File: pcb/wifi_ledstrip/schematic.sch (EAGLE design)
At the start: 44 parts, among them IC1 STM32F10XCXT6, Q1 8MHz

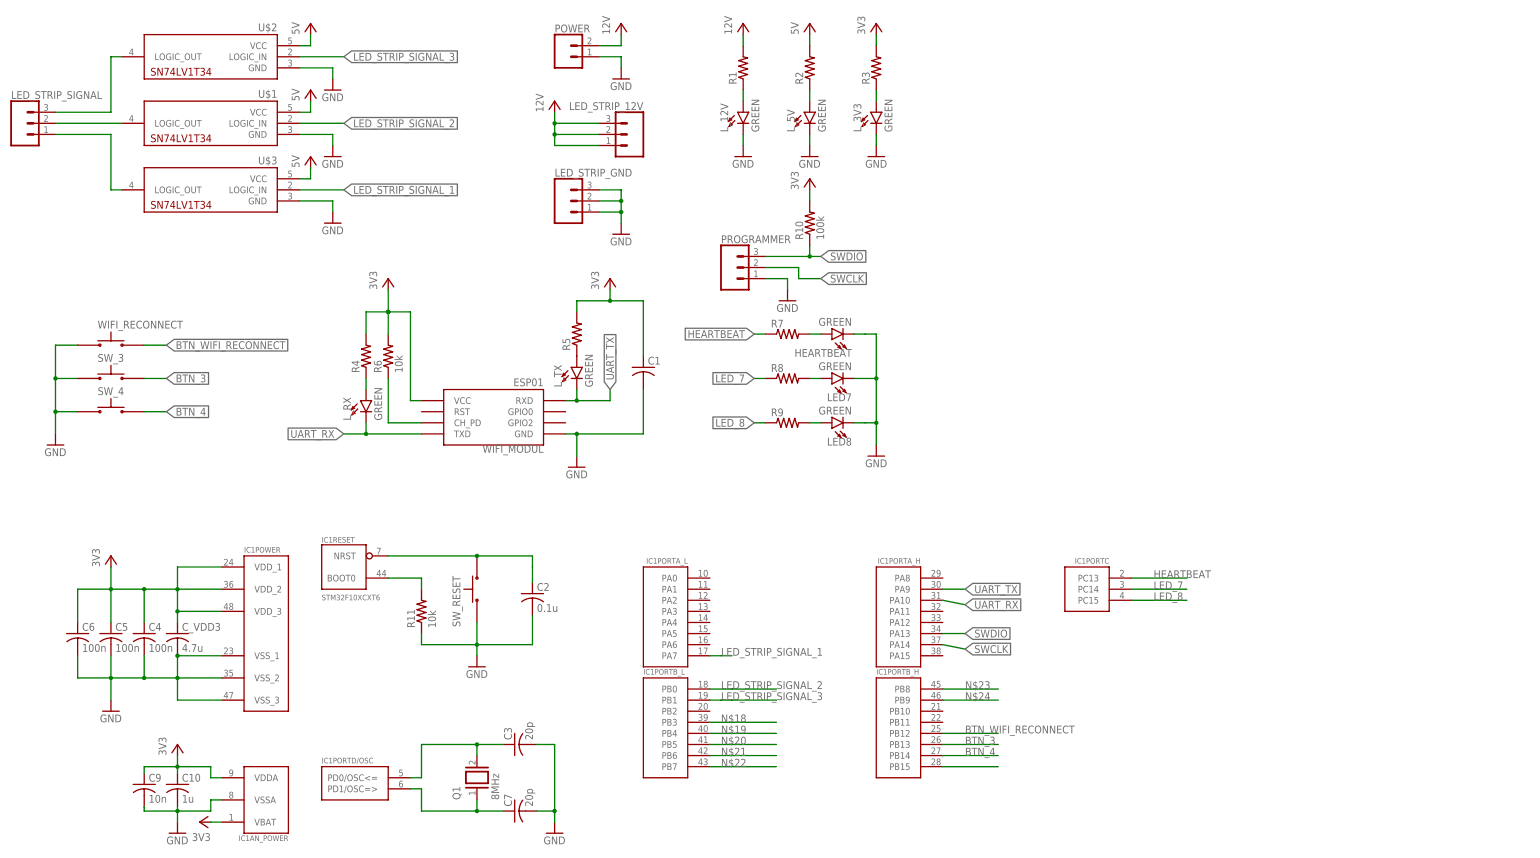
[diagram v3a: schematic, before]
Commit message: parts added, psu symbols fixed
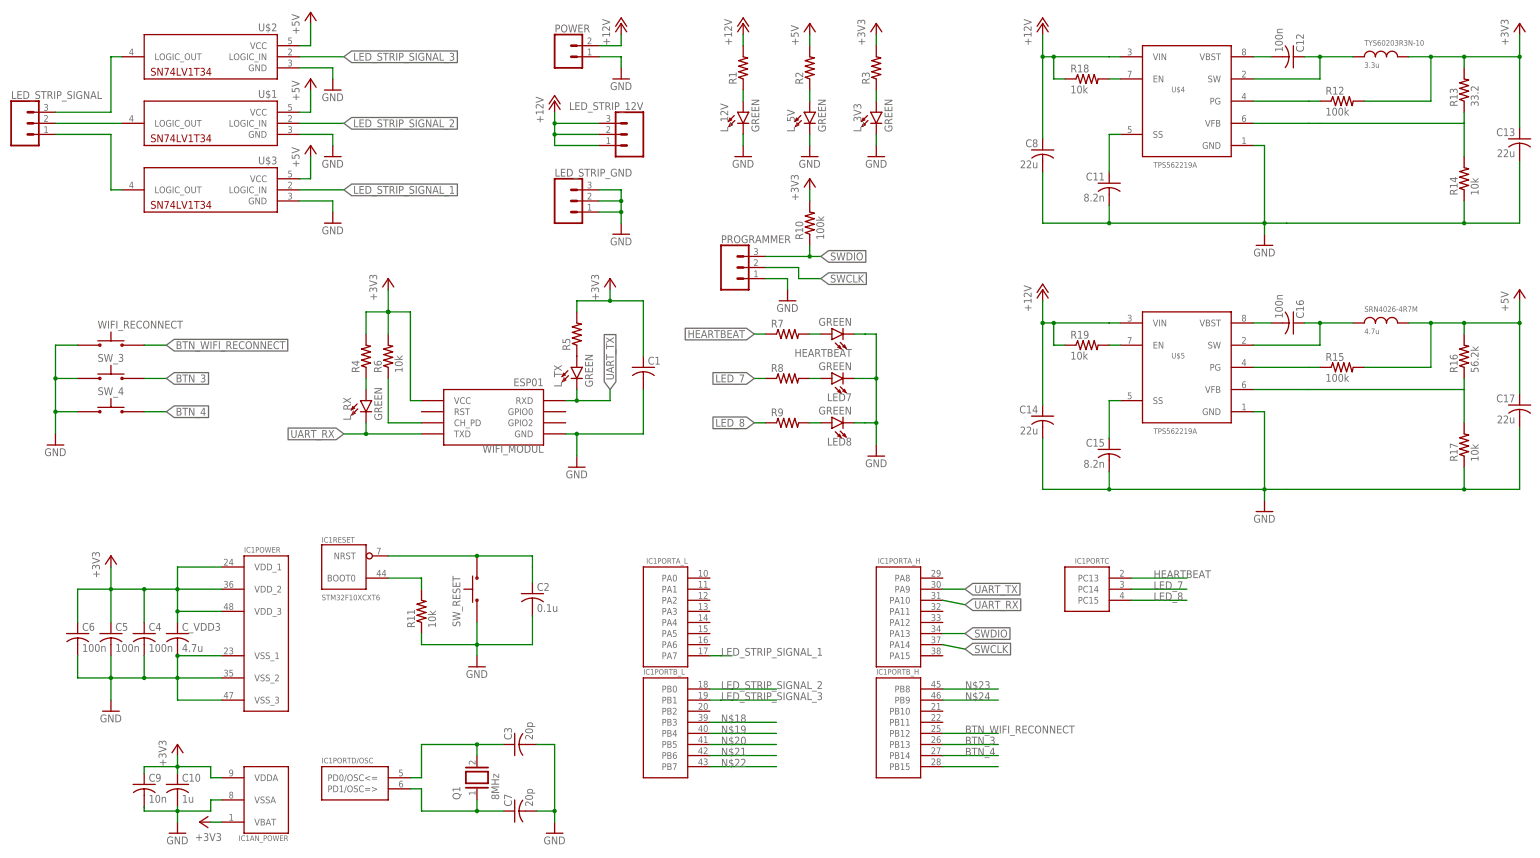
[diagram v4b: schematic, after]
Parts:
- added C11, C15: 8.2n, rcl:C-USC1206
- added C12, C16: 100n, rcl:C-USC1206
- added C13, C14, C17, C8: 22u, rcl:C-USC1206
- added R12, R15: 100k, rcl:R-US_R1206
- added R13: 33.2, rcl:R-US_R1206
- added R14, R17, R18, R19: 10k, rcl:R-US_R1206
- added R16: 56.2k, rcl:R-US_R1206
- added SRN4026-4R7M: 4.7u, mylibrary:SRN4026-4R7M
- added TYS60203R3N-10: 3.3u, mylibrary:TYS60203R3N-10
- added U$4, U$5: TPS562219A, mylibrary:TPS562219A
- U$2: SPICEPREFIX (none) -> U
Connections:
- removed net VCC: C1.1, C10.1, C4.1, C5.1, C6.1, C9.1, C_VDD3.1, IC1AN_POWER.VBAT, IC1AN_POWER.VDDA, IC1POWER.VDD_1, IC1POWER.VDD_2, IC1POWER.VDD_3, LED_STRIP_12V.1, LED_STRIP_12V.2, LED_STRIP_12V.3, POWER.2, R1.2, R10.2, R2.2, R3.2, R4.2, R5.2, R6.2, U$1.VCC, U$2.VCC, U$3.VCC, WIFI_MODUL.VCC
- new net +12V: C14.1, C8.1, LED_STRIP_12V.1, LED_STRIP_12V.2, LED_STRIP_12V.3, POWER.2, R1.2, R18.1, R19.1, U$4.VIN, U$5.VIN
- new net +3V3: C1.1, C10.1, C13.1, C4.1, C5.1, C6.1, C9.1, C_VDD3.1, IC1AN_POWER.VBAT, IC1AN_POWER.VDDA, IC1POWER.VDD_1, IC1POWER.VDD_2, IC1POWER.VDD_3, R10.2, R12.2, R13.2, R3.2, R4.2, R5.2, R6.2, TYS60203R3N-10.2, WIFI_MODUL.VCC
- new net +5V: C17.1, R15.2, R16.2, R2.2, SRN4026-4R7M.2, U$1.VCC, U$2.VCC, U$3.VCC
- new net N$17: C12.2, U$4.VBST
- new net N$25: C11.1, U$4.SS
- new net N$26: C12.1, TYS60203R3N-10.1, U$4.SW
- new net N$28: R12.1, U$4.PG
- new net N$29: U$4.VFB
- new net N$30: C15.1, U$5.SS
- new net N$31: C16.2, U$5.VBST
- new net N$32: R13.1, R14.2
- new net N$33: C16.1, SRN4026-4R7M.1, U$5.SW
- new net N$34: R15.1, U$5.PG
- new net N$35: U$5.VFB
- new net N$36: R16.1, R17.2
- new net N$37: R18.2, U$4.EN
- new net N$38: R19.2, U$5.EN
- net GND: now also C11.2, C13.2, C14.2, C15.2, C17.2, C8.2, R14.1, R17.1, U$4.GND, U$5.GND

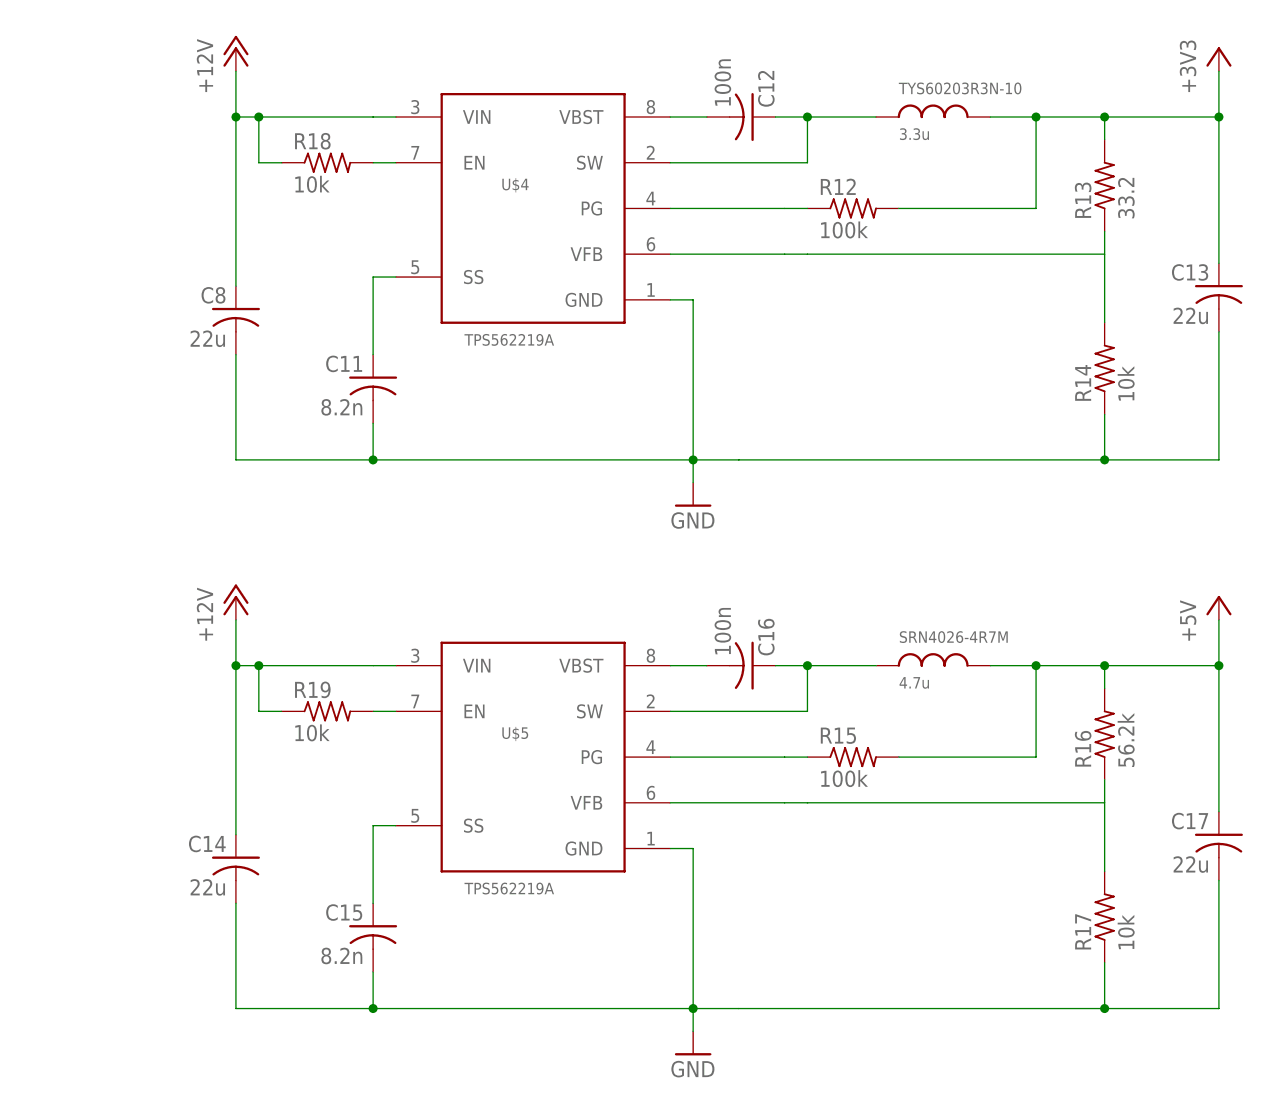
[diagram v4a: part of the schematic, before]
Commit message: psu 5v half ready
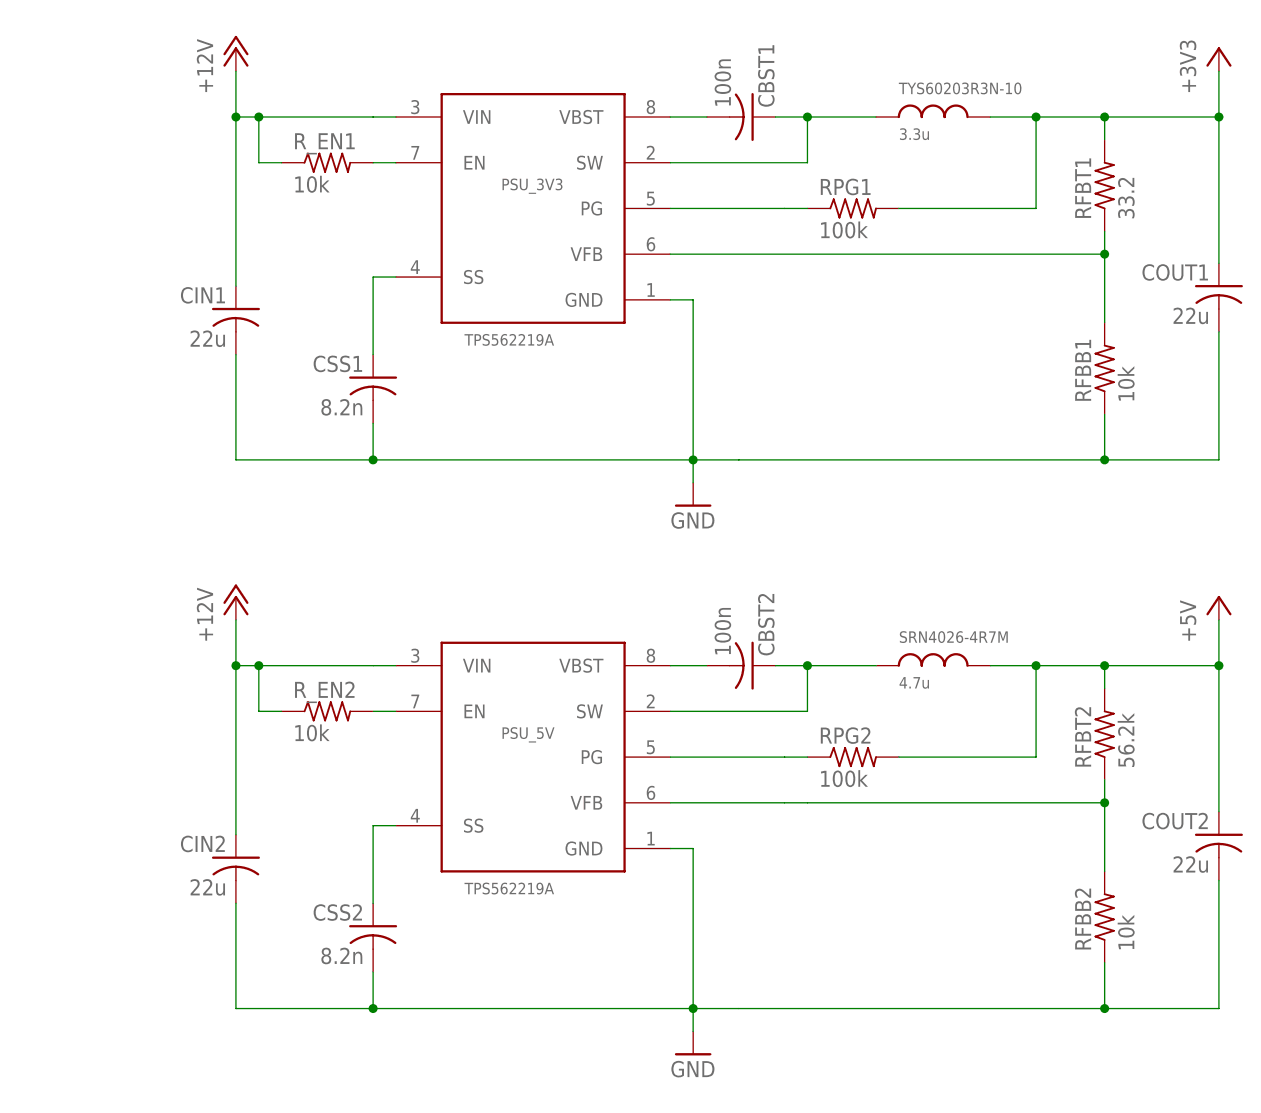
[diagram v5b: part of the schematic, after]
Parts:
- renumbered C11 to CSS1, C12 to CBST1, C13 to COUT1, C14 to CIN2, C15 to CSS2, C16 to CBST2, C17 to COUT2, C8 to CIN1, R12 to RPG1, R13 to RFBT1, R14 to RFBB1, R15 to RPG2, R16 to RFBT2, R17 to RFBB2, R18 to R_EN1, R19 to R_EN2, U$4 to PSU_3V3, U$5 to PSU_5V
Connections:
- removed net N$29: PSU_3V3.VFB
- removed net N$36: RFBB2.2, RFBT2.1
- net N$32: now also PSU_3V3.VFB
- net N$35: now also RFBB2.2, RFBT2.1

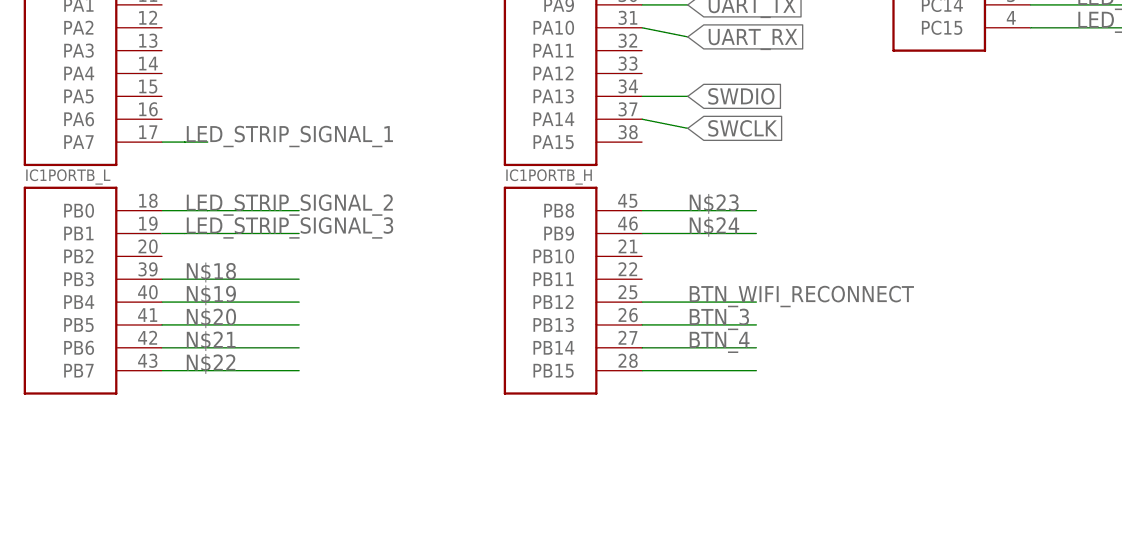
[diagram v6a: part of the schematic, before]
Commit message: beta pcb - resistor values need to be calculated
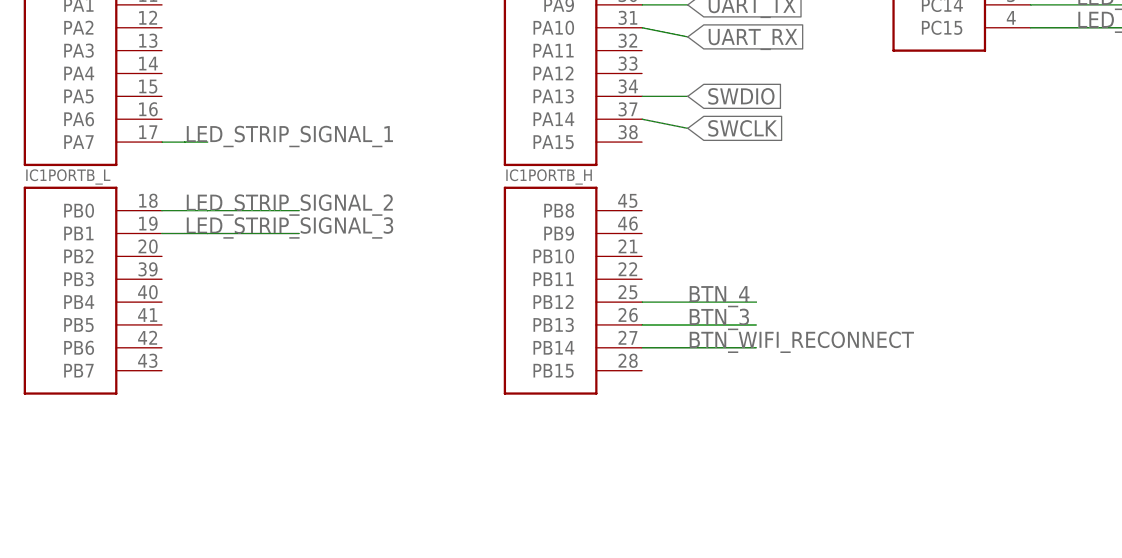
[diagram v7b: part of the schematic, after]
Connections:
- removed net N$18: IC1PORTB_L.PB3
- removed net N$19: IC1PORTB_L.PB4
- removed net N$20: IC1PORTB_L.PB5
- removed net N$21: IC1PORTB_L.PB6
- removed net N$22: IC1PORTB_L.PB7
- removed net N$23: IC1PORTB_H.PB8
- removed net N$24: IC1PORTB_H.PB9
- removed net N$27: IC1PORTB_H.PB15
- net BTN_4: now also IC1PORTB_H.PB12; no longer IC1PORTB_H.PB14
- net BTN_WIFI_RECONNECT: now also IC1PORTB_H.PB14; no longer IC1PORTB_H.PB12
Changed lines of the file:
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@@
+</segment>
+<segment>
+<pinref part="IC1" gate="PORTB_H" pin="PB14"/>
+<wire x1="220.98" y1="-76.2" x2="233.68" y2="-76.2" width="0.1524" layer="91"/>
+<label x="226.06" y="-76.2" size="1.778" layer="95"/>
+</segment>
+</net>
+<net name="BTN_3" class="0">
+<segment>
+<pinref part="SW_3" gate="&gt;NAME" pin="P$4"/>
+<wire x1="38.1" y1="10.16" x2="43.18" y2="10.16" width="0.1524" layer="91"/>
+<label x="43.18" y="10.16" size="1.778" layer="95" xref="yes"/>
+</segment>
+<segment>
+<pinref part="IC1" gate="PORTB_H" pin="PB13"/>
+<wire x1="220.98" y1="-73.66" x2="233.68" y2="-73.66" width="0.1524" layer="91"/>
+<label x="226.06" y="-73.66" size="1.778" layer="95"/>
+</segment>
+</net>
+<net name="BTN_4" class="0">
+<segment>
+<pinref part="SW_4" gate="&gt;NAME" pin="P$4"/>
+<wire x1="38.1" y1="2.54" x2="43.18" y2="2.54" width="0.1524" layer="91"/>
+<label x="43.18" y="2.54" size="1.778" layer="95" xref="yes"/>
 </segment>
 <segment>
@@
 <wire x1="220.98" y1="-71.12" x2="233.68" y2="-71.12" width="0.1524" layer="91"/>
 <label x="226.06" y="-71.12" size="1.778" layer="95"/>
-</segment>
-</net>
-<net name="BTN_3" class="0">
-<segment>
-<pinref part="SW_3" gate="&gt;NAME" pin="P$4"/>
-<wire x1="38.1" y1="10.16" x2="43.18" y2="10.16" width="0.1524" layer="91"/>
-<label x="43.18" y="10.16" size="1.778" layer="95" xref="yes"/>
-</segment>
-<segment>
-<pinref part="IC1" gate="PORTB_H" pin="PB13"/>
-<wire x1="220.98" y1="-73.66" x2="233.68" y2="-73.66" width="0.1524" layer="91"/>
-<label x="226.06" y="-73.66" size="1.778" layer="95"/>
-</segment>
-</net>
-<net name="BTN_4" class="0">
-<segment>
-<pinref part="SW_4" gate="&gt;NAME" pin="P$4"/>
-<wire x1="38.1" y1="2.54" x2="43.18" y2="2.54" width="0.1524" layer="91"/>
-<label x="43.18" y="2.54" size="1.778" layer="95" xref="yes"/>
-</segment>
-<segment>
-<pinref part="IC1" gate="PORTB_H" pin="PB14"/>
-<wire x1="220.98" y1="-76.2" x2="233.68" y2="-76.2" width="0.1524" layer="91"/>
-<label x="226.06" y="-76.2" size="1.778" layer="95"/>
 </segment>
 </net>
@@
 </segment>
 </net>
-<net name="N$18" class="0">
-<segment>
-<pinref part="IC1" gate="PORTB_L" pin="PB3"/>
-<wire x1="167.64" y1="-68.58" x2="182.88" y2="-68.58" width="0.1524" layer="91"/>
-<label x="170.18" y="-68.58" size="1.778" layer="95"/>
-</segment>
-</net>
-<net name="N$19" class="0">
-<segment>
-<pinref part="IC1" gate="PORTB_L" pin="PB4"/>
-<wire x1="167.64" y1="-71.12" x2="182.88" y2="-71.12" width="0.1524" layer="91"/>
-<label x="170.18" y="-71.12" size="1.778" layer="95"/>
-</segment>
-</net>
-<net name="N$20" class="0">
-<segment>
-<pinref part="IC1" gate="PORTB_L" pin="PB5"/>
-<wire x1="167.64" y1="-73.66" x2="182.88" y2="-73.66" width="0.1524" layer="91"/>
-<label x="170.18" y="-73.66" size="1.778" layer="95"/>
-</segment>
-</net>
-<net name="N$21" class="0">
-<segment>
-<pinref part="IC1" gate="PORTB_L" pin="PB6"/>
-<wire x1="167.64" y1="-76.2" x2="182.88" y2="-76.2" width="0.1524" layer="91"/>
-<label x="170.18" y="-76.2" size="1.778" layer="95"/>
-</segment>
-</net>
-<net name="N$22" class="0">
-<segment>
-<pinref part="IC1" gate="PORTB_L" pin="PB7"/>
-<wire x1="167.64" y1="-78.74" x2="182.88" y2="-78.74" width="0.1524" layer="91"/>
-<label x="170.18" y="-78.74" size="1.778" layer="95"/>
-</segment>
-</net>
-<net name="N$23" class="0">
-<segment>
-<pinref part="IC1" gate="PORTB_H" pin="PB8"/>
-<wire x1="220.98" y1="-60.96" x2="233.68" y2="-60.96" width="0.1524" layer="91"/>
-<label x="226.06" y="-60.96" size="1.778" layer="95"/>
-</segment>
-</net>
-<net name="N$24" class="0">
-<segment>
-<pinref part="IC1" gate="PORTB_H" pin="PB9"/>
-<wire x1="220.98" y1="-63.5" x2="233.68" y2="-63.5" width="0.1524" layer="91"/>
-<label x="226.06" y="-63.5" size="1.778" layer="95"/>
-</segment>
-</net>
-<net name="N$27" class="0">
-<segment>
-<pinref part="IC1" gate="PORTB_H" pin="PB15"/>
-<wire x1="220.98" y1="-78.74" x2="233.68" y2="-78.74" width="0.1524" layer="91"/>
-</segment>
-</net>
